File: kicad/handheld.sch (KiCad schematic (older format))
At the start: 23 parts, among them J1 Conn_01x08, J2 61300311121, J3 AVR-PDI-6, SW1 HOLD, SW2 PAUSE, SW3 SDROP, SW4 HDROP, SW5 ROTR, SW6 RIGHT, SW7 ROTL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

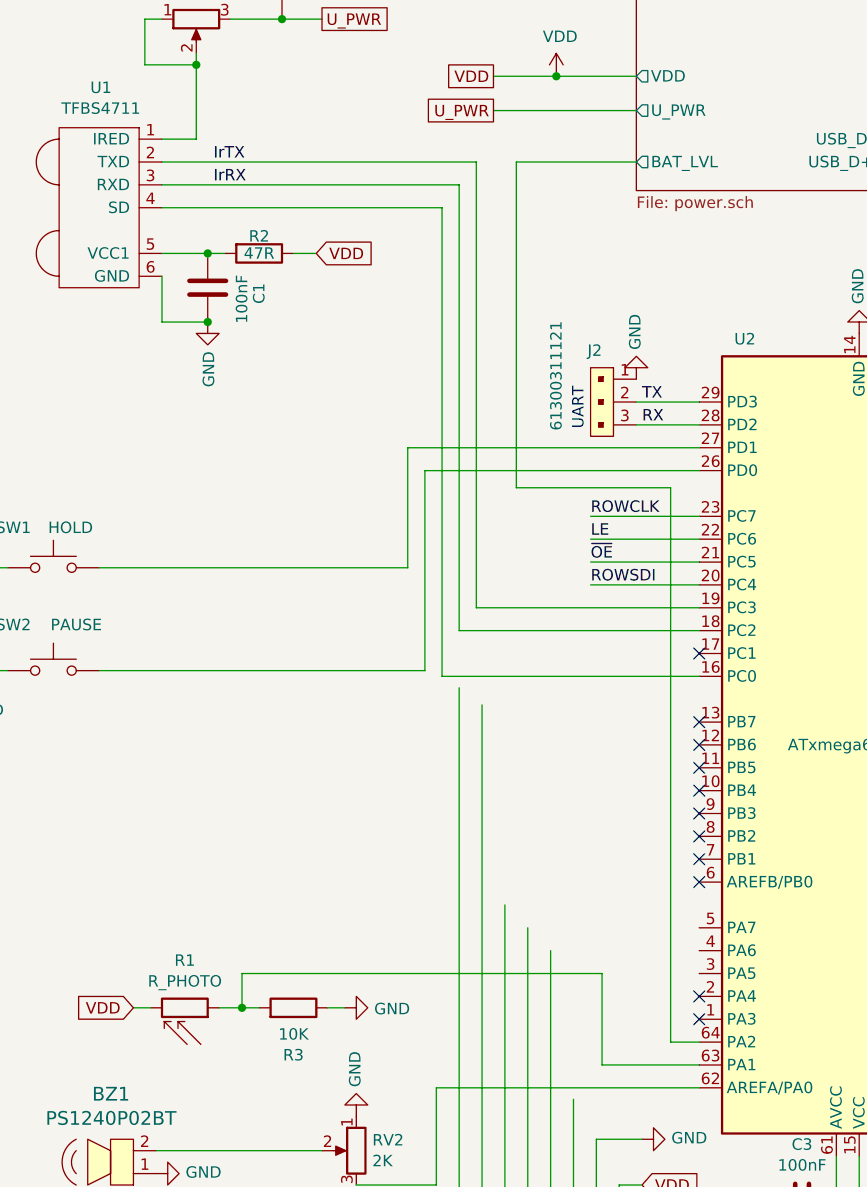
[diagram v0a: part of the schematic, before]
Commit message: Added power net and buck converter
Also wired up Ir transceiver.
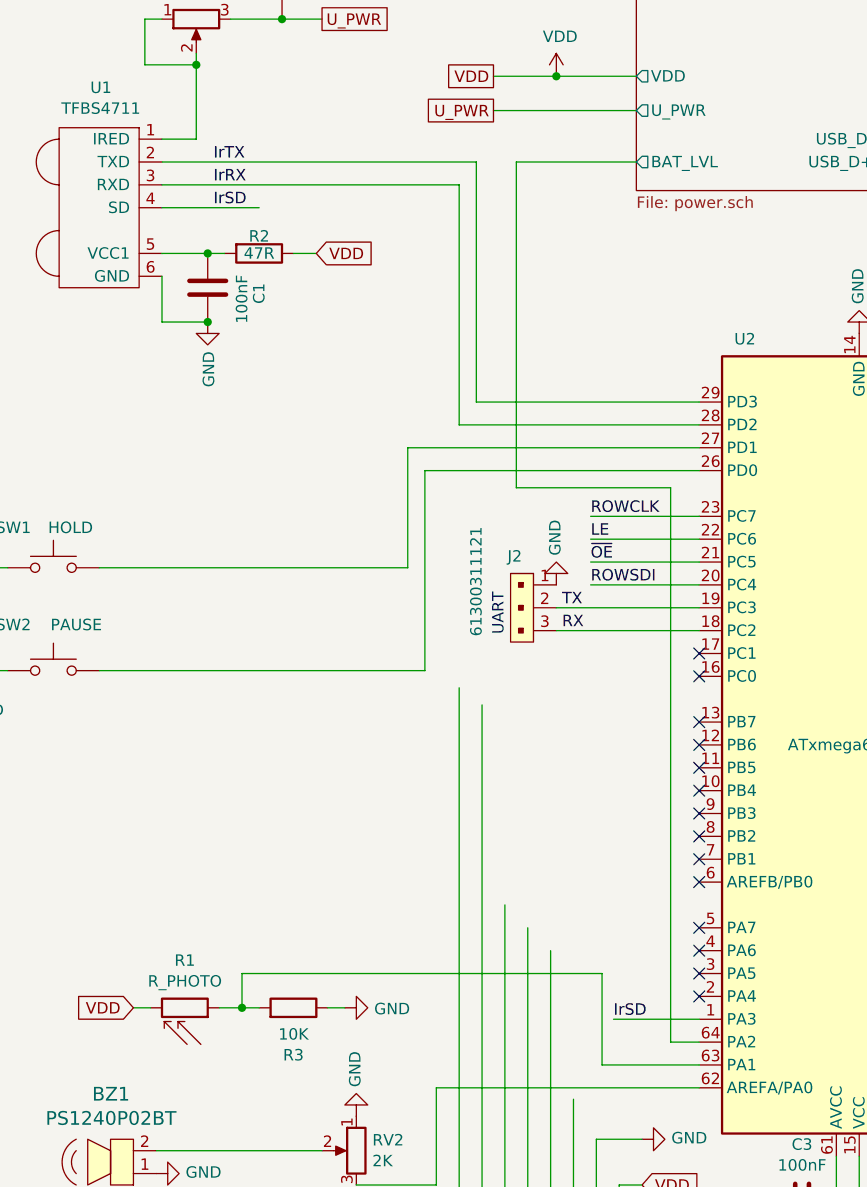
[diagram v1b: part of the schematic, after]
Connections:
- net labels added: IrSD
- wire segments 133 -> 132
- no-connect marks 14 -> 17
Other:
- moved on the sheet: J2
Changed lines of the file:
@@
 L dk_Rectangular-Connectors-Headers-Male-Pins:61300311121 J2
 U 1 1 5F933175
-P 3325 3075
-F 0 "J2" V 3200 3075 50  0000 R CNN
-F 1 "61300311121" H 3550 2875 50  0000 R CNN
-F 2 "Connector_PinSocket_2.54mm:PinSocket_1x03_P2.54mm_Horizontal" H 3525 3275 60  0001 L CNN
-F 3 "https://katalog.we-online.de/em/datasheet/6130xx11121.pdf" H 3525 3375 60  0001 L CNN
-F 4 "732-5316-ND" H 3525 3475 60  0001 L CNN "Digi-Key_PN"
-F 5 "61300311121" H 3525 3575 60  0001 L CNN "MPN"
-F 6 "Connectors, Interconnects" H 3525 3675 60  0001 L CNN "Category"
-F 7 "Rectangular Connectors - Headers, Male Pins" H 3525 3775 60  0001 L CNN "Family"
-F 8 "https://katalog.we-online.de/em/datasheet/6130xx11121.pdf" H 3525 3875 60  0001 L CNN "DK_Datasheet_Link"
-F 9 "/product-detail/en/wurth-electronics-inc/61300311121/732-5316-ND/4846825" H 3525 3975 60  0001 L CNN "DK_Detail_Page"
-F 10 "CONN HEADER VERT 3POS 2.54MM" H 3525 4075 60  0001 L CNN "Description"
-F 11 "Wurth Electronics Inc." H 3525 4175 60  0001 L CNN "Manufacturer"
-F 12 "Active" H 3525 4275 60  0001 L CNN "Status"
-	1    3325 3075
+P 2975 3975
+F 0 "J2" V 2850 3975 50  0000 R CNN
+F 1 "61300311121" H 3200 3775 50  0000 R CNN
+F 2 "Connector_PinSocket_2.54mm:PinSocket_1x03_P2.54mm_Horizontal" H 3175 4175 60  0001 L CNN
+F 3 "https://katalog.we-online.de/em/datasheet/6130xx11121.pdf" H 3175 4275 60  0001 L CNN
+F 4 "732-5316-ND" H 3175 4375 60  0001 L CNN "Digi-Key_PN"
+F 5 "61300311121" H 3175 4475 60  0001 L CNN "MPN"
+F 6 "Connectors, Interconnects" H 3175 4575 60  0001 L CNN "Category"
+F 7 "Rectangular Connectors - Headers, Male Pins" H 3175 4675 60  0001 L CNN "Family"
+F 8 "https://katalog.we-online.de/em/datasheet/6130xx11121.pdf" H 3175 4775 60  0001 L CNN "DK_Datasheet_Link"
+F 9 "/product-detail/en/wurth-electronics-inc/61300311121/732-5316-ND/4846825" H 3175 4875 60  0001 L CNN "DK_Detail_Page"
+F 10 "CONN HEADER VERT 3POS 2.54MM" H 3175 4975 60  0001 L CNN "Description"
+F 11 "Wurth Electronics Inc." H 3175 5075 60  0001 L CNN "Manufacturer"
+F 12 "Active" H 3175 5175 60  0001 L CNN "Status"
+	1    2975 3975
 	0    1    1    0
 $EndComp
 Wire Wire Line
-	3750 3275 3475 3275
+	3750 4175 3125 4175
 $Comp
 L power:GND #PWR08
 U 1 1 5F9AF30E
-P 3475 3075
-F 0 "#PWR08" H 3475 2825 50  0001 C CNN
-F 1 "GND" V 3480 2947 50  0000 R CNN
-F 2 "" H 3475 3075 50  0001 C CNN
-F 3 "" H 3475 3075 50  0001 C CNN
-	1    3475 3075
+P 3125 3975
+F 0 "#PWR08" H 3125 3725 50  0001 C CNN
+F 1 "GND" V 3130 3847 50  0000 R CNN
+F 2 "" H 3125 3975 50  0001 C CNN
+F 3 "" H 3125 3975 50  0001 C CNN
+	1    3125 3975
 	-1   0    0    1
 $EndComp
-Text Notes 3250 3300 1    50   ~ 0
+Text Notes 2900 4200 1    50   ~ 0
 UART
 Wire Wire Line
@@
 Connection ~ 5775 4875
 Wire Wire Line
-	3475 3175 3750 3175
-Text Label 3500 3275 0    50   ~ 0
+	3125 4075 3750 4075
+Text Label 3150 4175 0    50   ~ 0
 RX
-Text Label 3500 3175 0    50   ~ 0
+Text Label 3150 4075 0    50   ~ 0
 TX
 Wire Wire Line
@@
 Text GLabel 2075 2525 2    50   Input ~ 0
 VDD
-Wire Wire Line
-	2700 4175 3750 4175
-Wire Wire Line
-	2775 4075 3750 4075
-Wire Wire Line
-	2625 4375 3750 4375
 $Comp
 L Device:R R2
@@
 	1600 2525 1675 2525
 Wire Wire Line
-	1400 2325 2625 2325
-Wire Wire Line
-	2625 2325 2625 4375
-Wire Wire Line
 	1400 2225 2700 2225
 Wire Wire Line
-	2700 2225 2700 4175
-Wire Wire Line
 	1400 2125 2775 2125
-Wire Wire Line
-	2775 2125 2775 4075
 Wire Wire Line
 	1975 2525 2075 2525
@@
 	1925 1500 2100 1500
 NoConn ~ 3750 4275
-NoConn ~ 3750 5875
 $Comp
 L Connector_Generic:Conn_01x08 J1
@@
 Wire Wire Line
 	2600 6175 3750 6175
+Wire Wire Line
+	2700 2225 2700 3275
+Wire Wire Line
+	2700 3275 3750 3275
+Wire Wire Line
+	2775 2125 2775 3175
+Wire Wire Line
+	2775 3175 3750 3175
+Wire Wire Line
+	3750 5875 3375 5875
+Text Label 3375 5875 0    50   ~ 0
+IrSD
+Text Label 1625 2325 0    50   ~ 0
+IrSD
+Wire Wire Line
+	1400 2325 1825 2325
+NoConn ~ 3750 4375
+NoConn ~ 3750 5475
+NoConn ~ 3750 5575
+NoConn ~ 3750 5675
 Wire Bus Line
 	5775 4875 5775 5175

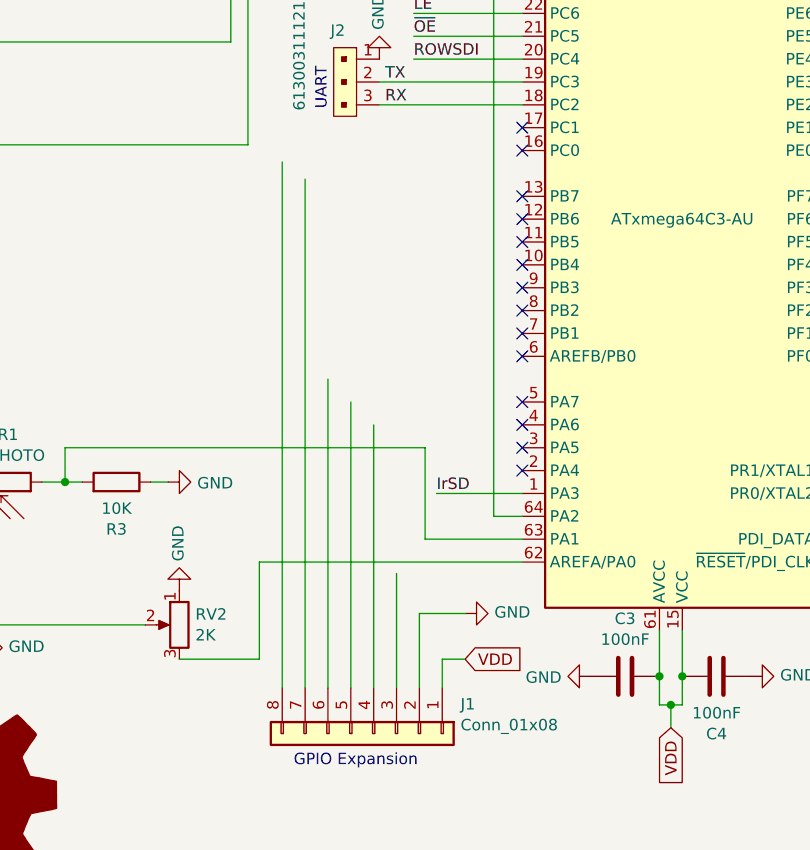
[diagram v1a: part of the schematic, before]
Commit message: Added GPIO expansion header
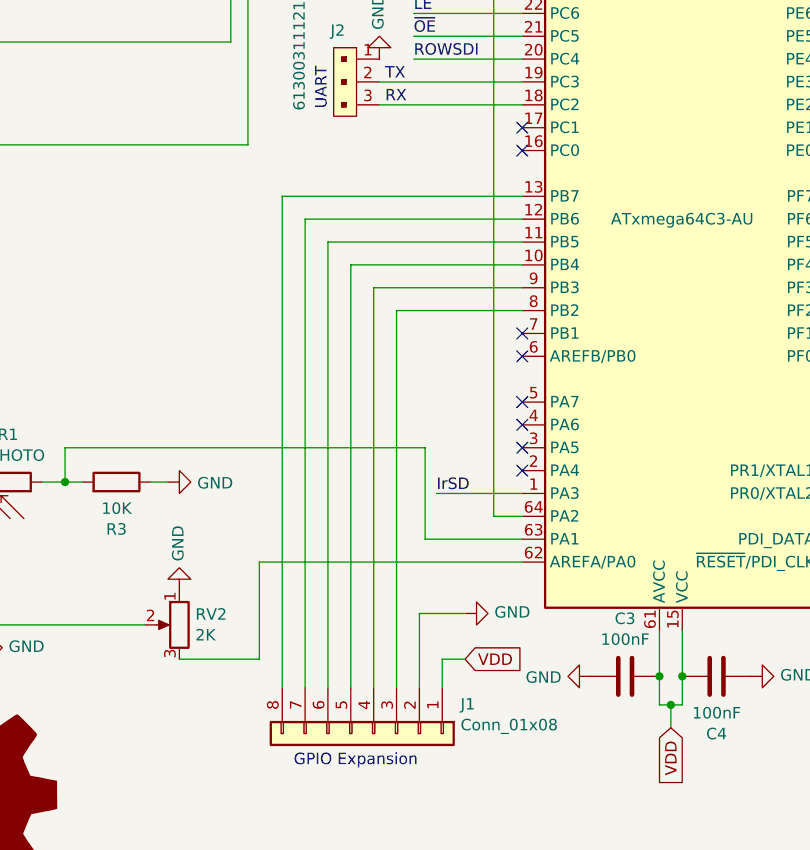
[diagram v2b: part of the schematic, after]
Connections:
- wire segments 132 -> 138
- no-connect marks 17 -> 11
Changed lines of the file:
@@
 	1925 1500 2100 1500
 NoConn ~ 3750 4275
-$Comp
-L Connector_Generic:Conn_01x08 J1
-U 1 1 5F91B7A4
-P 3100 6925
-F 0 "J1" V 2972 7305 50  0000 L CNN
-F 1 "Conn_01x08" V 3063 7305 50  0000 L CNN
-F 2 "Connector_PinSocket_2.54mm:PinSocket_1x08_P2.54mm_Horizontal" H 3100 6925 50  0001 C CNN
-F 3 "~" H 3100 6925 50  0001 C CNN
-	1    3100 6925
-	0    1    1    0
-$EndComp
-Text GLabel 3500 6600 2    50   Input ~ 0
-VDD
-Wire Wire Line
-	3400 6725 3400 6600
-Wire Wire Line
-	3400 6600 3500 6600
-$Comp
-L power:GND #PWR09
-U 1 1 5F922BBE
-P 3500 6400
-F 0 "#PWR09" H 3500 6150 50  0001 C CNN
-F 1 "GND" V 3505 6272 50  0000 R CNN
-F 2 "" H 3500 6400 50  0001 C CNN
-F 3 "" H 3500 6400 50  0001 C CNN
-	1    3500 6400
-	0    -1   -1   0
-$EndComp
-Wire Wire Line
-	3500 6400 3300 6400
-Wire Wire Line
-	3300 6400 3300 6725
-Wire Wire Line
-	3000 6725 3000 5475
-Wire Wire Line
-	3100 6725 3100 5575
-Wire Wire Line
-	3200 6725 3200 6225
 Wire Wire Line
 	3625 3550 3625 5975
@@
 Wire Wire Line
 	2950 3550 3625 3550
-Wire Wire Line
-	2700 4425 2700 6725
-Wire Wire Line
-	2800 4500 2800 6725
-Wire Wire Line
-	2900 5375 2900 6725
 Text Notes 2750 7075 0    50   ~ 0
 GPIO Expansion
@@
 	1125 4350 2550 4350
 Connection ~ 625  4350
-NoConn ~ 3750 4575
-NoConn ~ 3750 4675
-NoConn ~ 3750 4775
-NoConn ~ 3750 4875
-NoConn ~ 3750 4975
-NoConn ~ 3750 5075
-NoConn ~ 3750 5175
 NoConn ~ 3750 5275
 Wire Wire Line
@@
 NoConn ~ 3750 5575
 NoConn ~ 3750 5675
+Wire Wire Line
+	3300 6400 3300 6725
+Wire Wire Line
+	3500 6400 3300 6400
+$Comp
+L power:GND #PWR09
+U 1 1 5F922BBE
+P 3500 6400
+F 0 "#PWR09" H 3500 6150 50  0001 C CNN
+F 1 "GND" V 3505 6272 50  0000 R CNN
+F 2 "" H 3500 6400 50  0001 C CNN
+F 3 "" H 3500 6400 50  0001 C CNN
+	1    3500 6400
+	0    -1   -1   0
+$EndComp
+Wire Wire Line
+	3400 6600 3500 6600
+Wire Wire Line
+	3400 6725 3400 6600
+Text GLabel 3500 6600 2    50   Input ~ 0
+VDD
+$Comp
+L Connector_Generic:Conn_01x08 J1
+U 1 1 5F91B7A4
+P 3100 6925
+F 0 "J1" V 2972 7305 50  0000 L CNN
+F 1 "Conn_01x08" V 3063 7305 50  0000 L CNN
+F 2 "Connector_PinSocket_2.54mm:PinSocket_1x08_P2.54mm_Horizontal" H 3100 6925 50  0001 C CNN
+F 3 "~" H 3100 6925 50  0001 C CNN
+	1    3100 6925
+	0    1    1    0
+$EndComp
+Wire Wire Line
+	2700 4575 3750 4575
+Wire Wire Line
+	2700 4575 2700 6725
+Wire Wire Line
+	2800 4675 3750 4675
+Wire Wire Line
+	2800 4675 2800 6725
+Wire Wire Line
+	2900 4775 3750 4775
+Wire Wire Line
+	2900 4775 2900 6725
+Wire Wire Line
+	3000 4875 3750 4875
+Wire Wire Line
+	3000 4875 3000 6725
+Wire Wire Line
+	3100 4975 3750 4975
+Wire Wire Line
+	3100 4975 3100 6725
+Wire Wire Line
+	3200 5075 3750 5075
+Wire Wire Line
+	3200 5075 3200 6725
+NoConn ~ 3750 5175
 Wire Bus Line
 	5775 4875 5775 5175
